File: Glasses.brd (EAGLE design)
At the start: 147.4 x 68.7 mm, 254 parts, among them U1 APA1022020, U10 APA1022020, U100 APA1022020, U101 APA1022020, U102 APA1022020, U103 APA1022020, U104 APA1022020, U105 APA1022020, U106 APA1022020, U107 APA1022020, U108 APA1022020, U109 APA1022020, U11 APA1022020, U110 APA1022020, U111 APA1022020, U112 APA1022020, U113 APA1022020, U114 APA1022020, U115 APA1022020, U116 APA1022020, U117 APA1022020, U118 APA1022020, U119 APA1022020, U12 APA1022020, U120 APA1022020, U121 APA1022020, U122 APA1022020, U123 APA1022020, U124 APA1022020, U125 APA1022020, U126 APA1022020, U127 APA1022020, U128 APA1022020, U129 APA1022020, U13 APA1022020, U130 APA1022020, U131 APA1022020, U132 APA1022020, U133 APA1022020, U134 APA1022020, U135 APA1022020, U136 APA1022020, U137 APA1022020, U138 APA1022020, U139 APA1022020, U14 APA1022020, U140 APA1022020, U141 APA1022020, U142 APA1022020, U143 APA1022020, U144 APA1022020, U145 APA1022020, U146 APA1022020, U147 APA1022020, U148 APA1022020, U149 APA1022020, U15 APA1022020, U150 APA1022020, U151 APA1022020, U152 APA1022020, U153 APA1022020, U154 APA1022020, U155 APA1022020, U156 APA1022020, U157 APA1022020, U158 APA1022020, U159 APA1022020, U16 APA1022020, U160 APA1022020, U161 APA1022020, U162 APA1022020, U163 APA1022020, U164 APA1022020, U165 APA1022020, U166 APA1022020, U167 APA1022020, U168 APA1022020, U169 APA1022020, U17 APA1022020, U170 APA1022020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

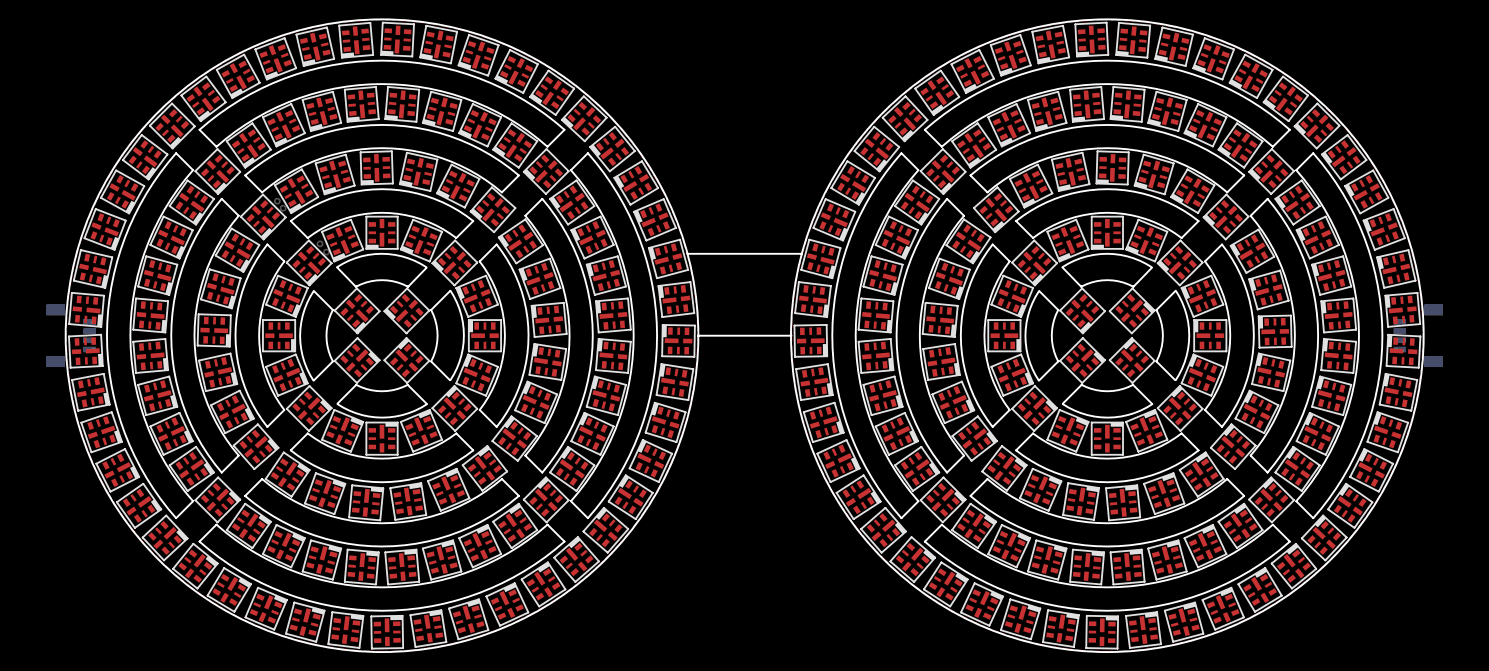
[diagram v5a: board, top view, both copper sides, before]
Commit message: Laid out most of board
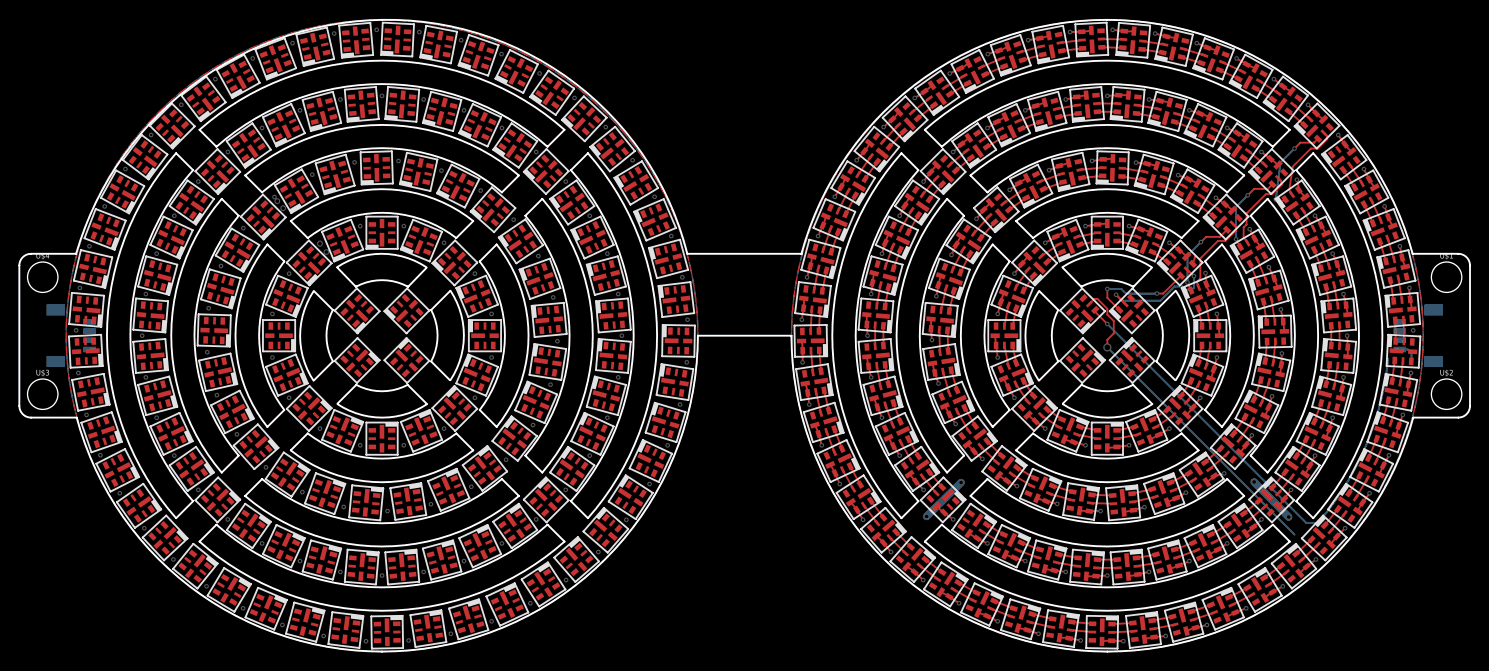
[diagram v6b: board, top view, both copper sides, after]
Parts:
- added U$1, U$2, U$3, U$4: (no value), SparkFun-Hardware:STAND-OFF
- moved J1 142.2 mm to (144.8, 34.3), turned to 270 degrees
- moved J2 142.2 mm to (2.54, 34.3), turned to 90 degrees
- moved U127 5.39 mm to (110.3, 37.0), turned to 45 degrees
- moved U129 5.39 mm to (115.7, 31.6), turned to 225 degrees
- moved U128 5.39 mm to (110.3, 31.6), turned to 135 degrees
- moved U130 5.39 mm to (115.7, 37.0), turned to 315 degrees
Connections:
- removed net N$491: J2.4, U252.CKO
- removed net N$492: J2.3, U252.SDO
- net N$269: now also J1.3
- net N$270: now also J2.3, U1.SDI; no longer J1.4, U126.CKO
- net N$423: now also U218.CKO, U219.CKI; no longer U219.SDI
- net N$424: now also U218.SDO, U219.SDI; no longer U219.CKI
- net N$477: now also U246.CKO, U247.CKI; no longer U247.SDI
- net N$478: now also U246.SDO, U247.SDI; no longer U247.CKI
- net N$489: now also J1.4
- net N$490: now also J2.4, U1.CKI; no longer J1.3, U126.SDO
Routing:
- net VCC: track 0.00 -> 280.1 mm, vias 0 -> 244
- net N$269: track 0.00 -> 53.3 mm, vias 0 -> 1
- net N$489: track 0.00 -> 38.2 mm, vias 0 -> 1
- net N$249: track 0.00 -> 13.3 mm, vias 0 -> 2
- net N$250: track 0.00 -> 11.9 mm, vias 0 -> 2
- net GND: track 0.00 -> 11.5 mm, vias 0 -> 4
- net N$400: track 0.00 -> 10.4 mm, vias 0 -> 2
- net N$329: track 0.00 -> 9.46 mm, vias 0 -> 2
- net N$330: track 0.00 -> 9.38 mm
- net N$282: track 0.00 -> 9.34 mm, vias 0 -> 2
- net N$281: track 0.00 -> 9.32 mm
- net N$399: track 0.00 -> 8.97 mm
- net N$296: track 0.00 -> 2.48 mm
- net N$299: track 0.00 -> 2.48 mm
- net N$310: track 0.00 -> 2.48 mm
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- added copper zone on layer 16, net VCC
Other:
- board size 147.4 x 68.7 mm -> 157.5 x 68.6 mm

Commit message: ordered v01
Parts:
- added FD1, FD2: FIDUCIALUFIDUCIAL, SparkFun-Aesthetics:FIDUCIAL-MICRO
- moved U238 0.13 mm to (121.3, 3.32)
- moved U112 0.13 mm to (65.3, 42.6)
- moved U223 0.13 mm to (82.1, 42.6)
- moved U97 0.13 mm to (26.0, 3.32)
- moved U27 0.13 mm to (20.7, 22.3)
- moved U40 0.13 mm to (46.3, 47.9)
- moved U153 0.13 mm to (101.1, 47.9)
- moved U166 0.13 mm to (126.6, 22.3)
- moved U252 0.13 mm to (138.6, 53.6)
- moved U83 0.13 mm to (8.68, 53.6)
- moved U126 0.13 mm to (15.0, 59.9)
- moved U209 0.13 mm to (132.3, 59.9)
- moved U37 0.13 mm to (52.3, 36.0)
- moved U163 0.13 mm to (114.7, 16.3)
- moved U30 0.13 mm to (32.6, 16.3)
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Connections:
- new net N$181: U95.SDO, U96.SDI
- new net N$182: U95.CKO, U96.CKI
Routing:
- net VCC: track 280.1 -> 600.3 mm, vias 244 -> 254
- net N$490: track 0.00 -> 65.9 mm, vias 0 -> 1
- net N$270: track 0.00 -> 53.5 mm, vias 0 -> 1
- net GND: track 11.5 -> 52.8 mm, vias 4 -> 22
- net N$489: track 38.2 -> 63.3 mm
- net N$8: track 0.00 -> 12.3 mm, vias 0 -> 2
- net N$7: track 0.00 -> 10.9 mm
- net N$154: track 0.00 -> 10.4 mm, vias 0 -> 2
- net N$85: track 0.00 -> 10.2 mm, vias 0 -> 2
- net N$38: track 0.00 -> 10.2 mm, vias 0 -> 2
- net N$86: track 0.00 -> 9.53 mm
- net N$153: track 0.00 -> 9.31 mm
- net N$37: track 0.00 -> 9.30 mm
- net N$6: track 0.00 -> 3.90 mm
- net N$3: track 0.00 -> 3.90 mm
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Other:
- outline, holes or cut-outs redrawn
- board text added: "Route out"
